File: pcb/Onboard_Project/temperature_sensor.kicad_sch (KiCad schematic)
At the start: 3 parts, among them U3 LM75ADP

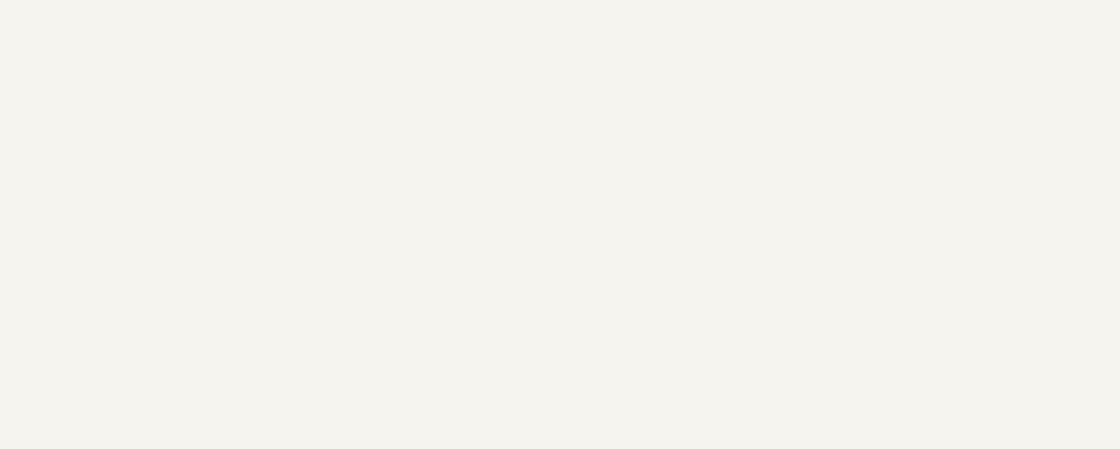
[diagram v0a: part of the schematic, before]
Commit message: Updating name & Color Sensor
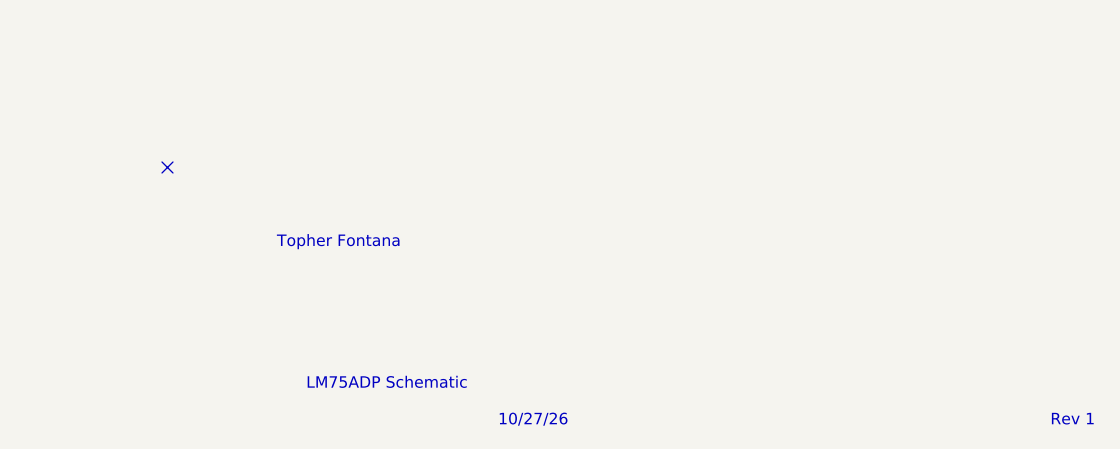
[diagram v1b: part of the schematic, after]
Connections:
- no-connect marks 0 -> 1
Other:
- note added: "10/27/26"
- note added: "LM75ADP Schematic"
- note added: "Rev 1"
- note added: "Topher Fontana"
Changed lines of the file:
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@@
 	(generator_version "10.0")
 	(paper "A4")
+	(text "Topher Fontana"
+		(exclude_from_sim no)
+		(at 191.77 173.482 0)
+		(effects
+			(font
+				(size 1.27 1.27)
+			)
+		)
+	)
+	(text "LM75ADP Schematic"
+		(exclude_from_sim no)
+		(at 197.104 189.23 0)
+		(effects
+			(font
+				(size 1.27 1.27)
+			)
+		)
+	)
+	(text "Rev 1"
+		(exclude_from_sim no)
+		(at 273.304 193.294 0)
+		(effects
+			(font
+				(size 1.27 1.27)
+			)
+		)
+	)
+	(text "10/27/26"
+		(exclude_from_sim no)
+		(at 213.36 193.294 0)
+		(effects
+			(font
+				(size 1.27 1.27)
+			)
+		)
+	)
 	(junction
 		(at 161.29 81.28)
@@
 		(diameter 0)
 		(color 0 0 0 0)
+	)
+	(no_connect
+		(at 172.72 165.1)
 	)
 	(bus_entry
@@
 		)
 		(instances
+			(project "temperature_sensor"
+				(path "/12ab8870-8aa2-4216-b652-4121a0b1f00c"
+					(reference "R7")
+					(unit 1)
+				)
+			)
 			(project "Onboadrd_Project"
 				(path "/c8ed4ef3-1d7f-4cb5-a0e2-1374e3f0f80e"
@@
 		)
 		(instances
+			(project "temperature_sensor"
+				(path "/12ab8870-8aa2-4216-b652-4121a0b1f00c"
+					(reference "#PWR060")
+					(unit 1)
+				)
+			)
 			(project "Onboadrd_Project"
 				(path "/c8ed4ef3-1d7f-4cb5-a0e2-1374e3f0f80e"
@@
 		)
 		(instances
+			(project "temperature_sensor"
+				(path "/12ab8870-8aa2-4216-b652-4121a0b1f00c"
+					(reference "U3")
+					(unit 1)
+				)
+			)
 			(project "Onboadrd_Project"
 				(path "/c8ed4ef3-1d7f-4cb5-a0e2-1374e3f0f80e"
@@
 		)
 		(instances
+			(project "temperature_sensor"
+				(path "/12ab8870-8aa2-4216-b652-4121a0b1f00c"
+					(reference "C18")
+					(unit 1)
+				)
+			)
 			(project "Onboadrd_Project"
 				(path "/c8ed4ef3-1d7f-4cb5-a0e2-1374e3f0f80e"
@@
 		)
 		(instances
+			(project "temperature_sensor"
+				(path "/12ab8870-8aa2-4216-b652-4121a0b1f00c"
+					(reference "#PWR058")
+					(unit 1)
+				)
+			)
 			(project "Onboadrd_Project"
 				(path "/c8ed4ef3-1d7f-4cb5-a0e2-1374e3f0f80e"
@@
 		)
 		(instances
+			(project "temperature_sensor"
+				(path "/12ab8870-8aa2-4216-b652-4121a0b1f00c"
+					(reference "#PWR063")
+					(unit 1)
+				)
+			)
 			(project "Onboadrd_Project"
 				(path "/c8ed4ef3-1d7f-4cb5-a0e2-1374e3f0f80e"
@@
 		)
 		(instances
+			(project "temperature_sensor"
+				(path "/12ab8870-8aa2-4216-b652-4121a0b1f00c"
+					(reference "#PWR059")
+					(unit 1)
+				)
+			)
 			(project "Onboadrd_Project"
 				(path "/c8ed4ef3-1d7f-4cb5-a0e2-1374e3f0f80e"
@@
 		)
 		(instances
+			(project "temperature_sensor"
+				(path "/12ab8870-8aa2-4216-b652-4121a0b1f00c"
+					(reference "#PWR062")
+					(unit 1)
+				)
+			)
 			(project "Onboadrd_Project"
 				(path "/c8ed4ef3-1d7f-4cb5-a0e2-1374e3f0f80e"
@@
 		)
 		(instances
+			(project "temperature_sensor"
+				(path "/12ab8870-8aa2-4216-b652-4121a0b1f00c"
+					(reference "#PWR064")
+					(unit 1)
+				)
+			)
 			(project "Onboadrd_Project"
 				(path "/c8ed4ef3-1d7f-4cb5-a0e2-1374e3f0f80e"
@@
 		)
 		(instances
+			(project "temperature_sensor"
+				(path "/12ab8870-8aa2-4216-b652-4121a0b1f00c"
+					(reference "#PWR061")
+					(unit 1)
+				)
+			)
 			(project "Onboadrd_Project"
 				(path "/c8ed4ef3-1d7f-4cb5-a0e2-1374e3f0f80e"
@@
 		)
 	)
+	(embedded_fonts no)
 )
